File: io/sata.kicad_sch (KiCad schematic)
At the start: 9 parts

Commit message: Sata schematic location fix
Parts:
- renumbered J to J?
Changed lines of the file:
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@@
 		(dnp no)
 		(fields_autoplaced yes)
-		(property "Reference" "J"
+		(property "Reference" "J?"
 			(at 129.54 62.2299 0)
 			(effects
@@
 		(instances
 			(project "Mantaray"
+				(path "/16640ecb-e4a4-4594-871b-70047bfba6e0/cc308790-ec7c-4071-93af-221aae7f0fb4/6ec1175a-a533-45d1-992f-35a75dc24d62"
+					(reference "J?")
+					(unit 1)
+				)
 				(path "/16640ecb-e4a4-4594-871b-70047bfba6e0/cc308790-ec7c-4071-93af-221aae7f0fb4/e1e652e7-0577-4d2a-87ec-23058b2a32e6"
 					(reference "J10")

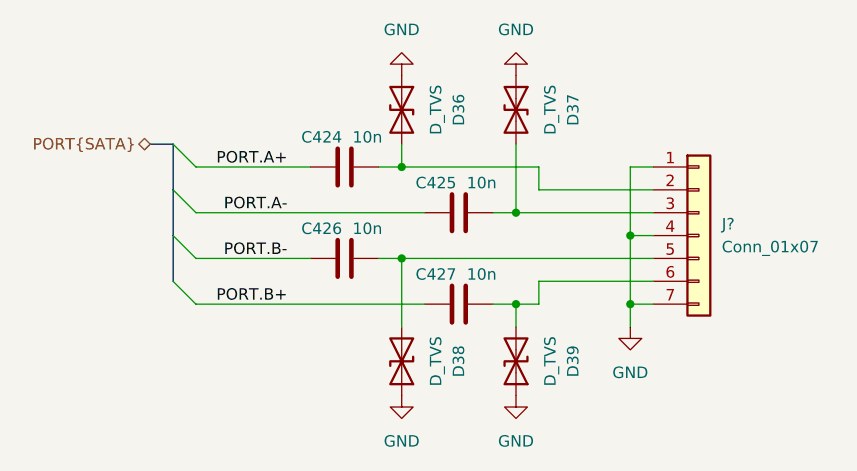
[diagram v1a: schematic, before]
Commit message: Multipurpose and standby power rails, Reannotated schematic
Added V_1P2, V_1P8, V_5P0DUAL, V_EFUSE, V_GPUPCIE, V_3P3STBY and V_1P2STBY
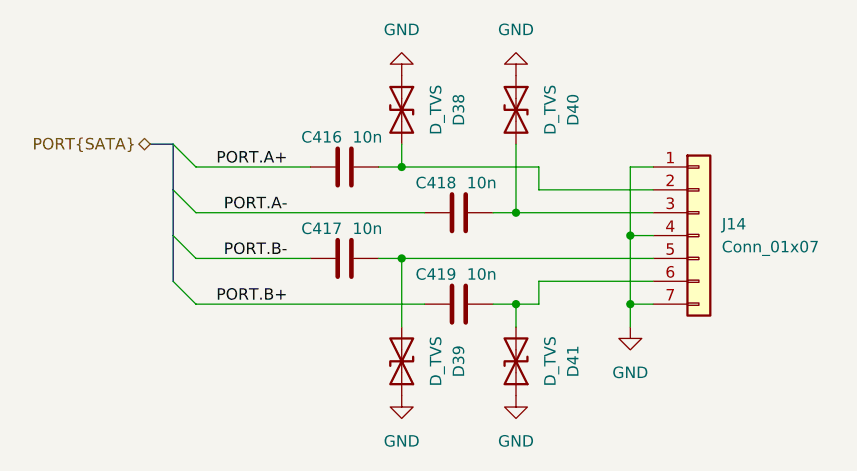
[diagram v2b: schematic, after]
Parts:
- gave numbers to parts that had none: 1
- renumbered C424 to C416, C426 to C417, C425 to C418, C427 to C419, D36 to D38, D38 to D39, D37 to D40, D39 to D41
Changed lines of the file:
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@@
 		(on_board yes)
 		(dnp no)
-		(property "Reference" "#PWR01"
+		(property "Reference" "#PWR0387"
 			(at 93.98 39.37 0)
 			(effects
@@
 			(project "Mantaray"
 				(path "/16640ecb-e4a4-4594-871b-70047bfba6e0/cc308790-ec7c-4071-93af-221aae7f0fb4/6ec1175a-a533-45d1-992f-35a75dc24d62"
-					(reference "#PWR01")
-					(unit 1)
-				)
-				(path "/16640ecb-e4a4-4594-871b-70047bfba6e0/cc308790-ec7c-4071-93af-221aae7f0fb4/e1e652e7-0577-4d2a-87ec-23058b2a32e6"
-					(reference "#PWR0393")
+					(reference "#PWR0387")
+					(unit 1)
+				)
+				(path "/16640ecb-e4a4-4594-871b-70047bfba6e0/cc308790-ec7c-4071-93af-221aae7f0fb4/e1e652e7-0577-4d2a-87ec-23058b2a32e6"
+					(reference "#PWR0392")
 					(unit 1)
 				)
@@
 		(on_board yes)
 		(dnp no)
-		(property "Reference" "D38"
+		(property "Reference" "D39"
 			(at 100.33 77.47 0)
 			(effects
@@
 			(project "Mantaray"
 				(path "/16640ecb-e4a4-4594-871b-70047bfba6e0/cc308790-ec7c-4071-93af-221aae7f0fb4/6ec1175a-a533-45d1-992f-35a75dc24d62"
-					(reference "D38")
-					(unit 1)
-				)
-				(path "/16640ecb-e4a4-4594-871b-70047bfba6e0/cc308790-ec7c-4071-93af-221aae7f0fb4/e1e652e7-0577-4d2a-87ec-23058b2a32e6"
-					(reference "D41")
+					(reference "D39")
+					(unit 1)
+				)
+				(path "/16640ecb-e4a4-4594-871b-70047bfba6e0/cc308790-ec7c-4071-93af-221aae7f0fb4/e1e652e7-0577-4d2a-87ec-23058b2a32e6"
+					(reference "D43")
 					(unit 1)
 				)
@@
 		(on_board yes)
 		(dnp no)
-		(property "Reference" "D37"
+		(property "Reference" "D40"
 			(at 113.03 49.53 0)
 			(effects
@@
 			(project "Mantaray"
 				(path "/16640ecb-e4a4-4594-871b-70047bfba6e0/cc308790-ec7c-4071-93af-221aae7f0fb4/6ec1175a-a533-45d1-992f-35a75dc24d62"
-					(reference "D37")
-					(unit 1)
-				)
-				(path "/16640ecb-e4a4-4594-871b-70047bfba6e0/cc308790-ec7c-4071-93af-221aae7f0fb4/e1e652e7-0577-4d2a-87ec-23058b2a32e6"
-					(reference "D42")
+					(reference "D40")
+					(unit 1)
+				)
+				(path "/16640ecb-e4a4-4594-871b-70047bfba6e0/cc308790-ec7c-4071-93af-221aae7f0fb4/e1e652e7-0577-4d2a-87ec-23058b2a32e6"
+					(reference "D44")
 					(unit 1)
 				)
@@
 		(on_board yes)
 		(dnp no)
-		(property "Reference" "C425"
+		(property "Reference" "C418"
 			(at 97.79 57.658 90)
 			(effects
@@
 			(project "Mantaray"
 				(path "/16640ecb-e4a4-4594-871b-70047bfba6e0/cc308790-ec7c-4071-93af-221aae7f0fb4/6ec1175a-a533-45d1-992f-35a75dc24d62"
-					(reference "C425")
-					(unit 1)
-				)
-				(path "/16640ecb-e4a4-4594-871b-70047bfba6e0/cc308790-ec7c-4071-93af-221aae7f0fb4/e1e652e7-0577-4d2a-87ec-23058b2a32e6"
-					(reference "C430")
+					(reference "C418")
+					(unit 1)
+				)
+				(path "/16640ecb-e4a4-4594-871b-70047bfba6e0/cc308790-ec7c-4071-93af-221aae7f0fb4/e1e652e7-0577-4d2a-87ec-23058b2a32e6"
+					(reference "C422")
 					(unit 1)
 				)
@@
 		(on_board yes)
 		(dnp no)
-		(property "Reference" "C426"
+		(property "Reference" "C417"
 			(at 85.09 62.738 90)
 			(effects
@@
 			(project "Mantaray"
 				(path "/16640ecb-e4a4-4594-871b-70047bfba6e0/cc308790-ec7c-4071-93af-221aae7f0fb4/6ec1175a-a533-45d1-992f-35a75dc24d62"
-					(reference "C426")
-					(unit 1)
-				)
-				(path "/16640ecb-e4a4-4594-871b-70047bfba6e0/cc308790-ec7c-4071-93af-221aae7f0fb4/e1e652e7-0577-4d2a-87ec-23058b2a32e6"
-					(reference "C429")
+					(reference "C417")
+					(unit 1)
+				)
+				(path "/16640ecb-e4a4-4594-871b-70047bfba6e0/cc308790-ec7c-4071-93af-221aae7f0fb4/e1e652e7-0577-4d2a-87ec-23058b2a32e6"
+					(reference "C421")
 					(unit 1)
 				)
@@
 		(on_board yes)
 		(dnp no)
-		(property "Reference" "#PWR0391"
+		(property "Reference" "#PWR0390"
 			(at 106.68 87.63 0)
 			(effects
@@
 			(project "Mantaray"
 				(path "/16640ecb-e4a4-4594-871b-70047bfba6e0/cc308790-ec7c-4071-93af-221aae7f0fb4/6ec1175a-a533-45d1-992f-35a75dc24d62"
-					(reference "#PWR0391")
-					(unit 1)
-				)
-				(path "/16640ecb-e4a4-4594-871b-70047bfba6e0/cc308790-ec7c-4071-93af-221aae7f0fb4/e1e652e7-0577-4d2a-87ec-23058b2a32e6"
-					(reference "#PWR0396")
+					(reference "#PWR0390")
+					(unit 1)
+				)
+				(path "/16640ecb-e4a4-4594-871b-70047bfba6e0/cc308790-ec7c-4071-93af-221aae7f0fb4/e1e652e7-0577-4d2a-87ec-23058b2a32e6"
+					(reference "#PWR0395")
 					(unit 1)
 				)
@@
 		(on_board yes)
 		(dnp no)
-		(property "Reference" "#PWR0390"
+		(property "Reference" "#PWR0388"
 			(at 93.98 87.63 0)
 			(effects
@@
 			(project "Mantaray"
 				(path "/16640ecb-e4a4-4594-871b-70047bfba6e0/cc308790-ec7c-4071-93af-221aae7f0fb4/6ec1175a-a533-45d1-992f-35a75dc24d62"
-					(reference "#PWR0390")
-					(unit 1)
-				)
-				(path "/16640ecb-e4a4-4594-871b-70047bfba6e0/cc308790-ec7c-4071-93af-221aae7f0fb4/e1e652e7-0577-4d2a-87ec-23058b2a32e6"
-					(reference "#PWR0394")
+					(reference "#PWR0388")
+					(unit 1)
+				)
+				(path "/16640ecb-e4a4-4594-871b-70047bfba6e0/cc308790-ec7c-4071-93af-221aae7f0fb4/e1e652e7-0577-4d2a-87ec-23058b2a32e6"
+					(reference "#PWR0393")
 					(unit 1)
 				)
@@
 		(on_board yes)
 		(dnp no)
-		(property "Reference" "C427"
+		(property "Reference" "C419"
 			(at 97.79 67.818 90)
 			(effects
@@
 			(project "Mantaray"
 				(path "/16640ecb-e4a4-4594-871b-70047bfba6e0/cc308790-ec7c-4071-93af-221aae7f0fb4/6ec1175a-a533-45d1-992f-35a75dc24d62"
-					(reference "C427")
-					(unit 1)
-				)
-				(path "/16640ecb-e4a4-4594-871b-70047bfba6e0/cc308790-ec7c-4071-93af-221aae7f0fb4/e1e652e7-0577-4d2a-87ec-23058b2a32e6"
-					(reference "C431")
+					(reference "C419")
+					(unit 1)
+				)
+				(path "/16640ecb-e4a4-4594-871b-70047bfba6e0/cc308790-ec7c-4071-93af-221aae7f0fb4/e1e652e7-0577-4d2a-87ec-23058b2a32e6"
+					(reference "C423")
 					(unit 1)
 				)
@@
 		(dnp no)
 		(fields_autoplaced yes)
-		(property "Reference" "J?"
+		(property "Reference" "J14"
 			(at 129.54 62.2299 0)
 			(effects
@@
 			(project "Mantaray"
 				(path "/16640ecb-e4a4-4594-871b-70047bfba6e0/cc308790-ec7c-4071-93af-221aae7f0fb4/6ec1175a-a533-45d1-992f-35a75dc24d62"
-					(reference "J?")
-					(unit 1)
-				)
-				(path "/16640ecb-e4a4-4594-871b-70047bfba6e0/cc308790-ec7c-4071-93af-221aae7f0fb4/e1e652e7-0577-4d2a-87ec-23058b2a32e6"
-					(reference "J10")
+					(reference "J14")
+					(unit 1)
+				)
+				(path "/16640ecb-e4a4-4594-871b-70047bfba6e0/cc308790-ec7c-4071-93af-221aae7f0fb4/e1e652e7-0577-4d2a-87ec-23058b2a32e6"
+					(reference "J15")
 					(unit 1)
 				)
@@
 		(on_board yes)
 		(dnp no)
-		(property "Reference" "D36"
+		(property "Reference" "D38"
 			(at 100.33 49.53 0)
 			(effects
@@
 			(project "Mantaray"
 				(path "/16640ecb-e4a4-4594-871b-70047bfba6e0/cc308790-ec7c-4071-93af-221aae7f0fb4/6ec1175a-a533-45d1-992f-35a75dc24d62"
-					(reference "D36")
-					(unit 1)
-				)
-				(path "/16640ecb-e4a4-4594-871b-70047bfba6e0/cc308790-ec7c-4071-93af-221aae7f0fb4/e1e652e7-0577-4d2a-87ec-23058b2a32e6"
-					(reference "D40")
+					(reference "D38")
+					(unit 1)
+				)
+				(path "/16640ecb-e4a4-4594-871b-70047bfba6e0/cc308790-ec7c-4071-93af-221aae7f0fb4/e1e652e7-0577-4d2a-87ec-23058b2a32e6"
+					(reference "D42")
 					(unit 1)
 				)
@@
 		(on_board yes)
 		(dnp no)
-		(property "Reference" "C424"
+		(property "Reference" "C416"
 			(at 85.09 52.578 90)
 			(effects
@@
 			(project "Mantaray"
 				(path "/16640ecb-e4a4-4594-871b-70047bfba6e0/cc308790-ec7c-4071-93af-221aae7f0fb4/6ec1175a-a533-45d1-992f-35a75dc24d62"
-					(reference "C424")
-					(unit 1)
-				)
-				(path "/16640ecb-e4a4-4594-871b-70047bfba6e0/cc308790-ec7c-4071-93af-221aae7f0fb4/e1e652e7-0577-4d2a-87ec-23058b2a32e6"
-					(reference "C428")
+					(reference "C416")
+					(unit 1)
+				)
+				(path "/16640ecb-e4a4-4594-871b-70047bfba6e0/cc308790-ec7c-4071-93af-221aae7f0fb4/e1e652e7-0577-4d2a-87ec-23058b2a32e6"
+					(reference "C420")
 					(unit 1)
 				)
@@
 		(on_board yes)
 		(dnp no)
-		(property "Reference" "#PWR0392"
+		(property "Reference" "#PWR0391"
 			(at 119.38 80.01 0)
 			(effects
@@
 			(project "Mantaray"
 				(path "/16640ecb-e4a4-4594-871b-70047bfba6e0/cc308790-ec7c-4071-93af-221aae7f0fb4/6ec1175a-a533-45d1-992f-35a75dc24d62"
-					(reference "#PWR0392")
-					(unit 1)
-				)
-				(path "/16640ecb-e4a4-4594-871b-70047bfba6e0/cc308790-ec7c-4071-93af-221aae7f0fb4/e1e652e7-0577-4d2a-87ec-23058b2a32e6"
-					(reference "#PWR0397")
+					(reference "#PWR0391")
+					(unit 1)
+				)
+				(path "/16640ecb-e4a4-4594-871b-70047bfba6e0/cc308790-ec7c-4071-93af-221aae7f0fb4/e1e652e7-0577-4d2a-87ec-23058b2a32e6"
+					(reference "#PWR0396")
 					(unit 1)
 				)
@@
 		(on_board yes)
 		(dnp no)
-		(property "Reference" "D39"
+		(property "Reference" "D41"
 			(at 113.03 77.47 0)
 			(effects
@@
 			(project "Mantaray"
 				(path "/16640ecb-e4a4-4594-871b-70047bfba6e0/cc308790-ec7c-4071-93af-221aae7f0fb4/6ec1175a-a533-45d1-992f-35a75dc24d62"
-					(reference "D39")
-					(unit 1)
-				)
-				(path "/16640ecb-e4a4-4594-871b-70047bfba6e0/cc308790-ec7c-4071-93af-221aae7f0fb4/e1e652e7-0577-4d2a-87ec-23058b2a32e6"
-					(reference "D43")
+					(reference "D41")
+					(unit 1)
+				)
+				(path "/16640ecb-e4a4-4594-871b-70047bfba6e0/cc308790-ec7c-4071-93af-221aae7f0fb4/e1e652e7-0577-4d2a-87ec-23058b2a32e6"
+					(reference "D45")
 					(unit 1)
 				)
@@
 				)
 				(path "/16640ecb-e4a4-4594-871b-70047bfba6e0/cc308790-ec7c-4071-93af-221aae7f0fb4/e1e652e7-0577-4d2a-87ec-23058b2a32e6"
-					(reference "#PWR0395")
-					(unit 1)
-				)
+					(reference "#PWR0394")
+					(unit 1)
+				)
